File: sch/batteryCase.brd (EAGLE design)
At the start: 68.2 x 27.9 mm, 7 parts, among them X1 C-GRID-04-70553

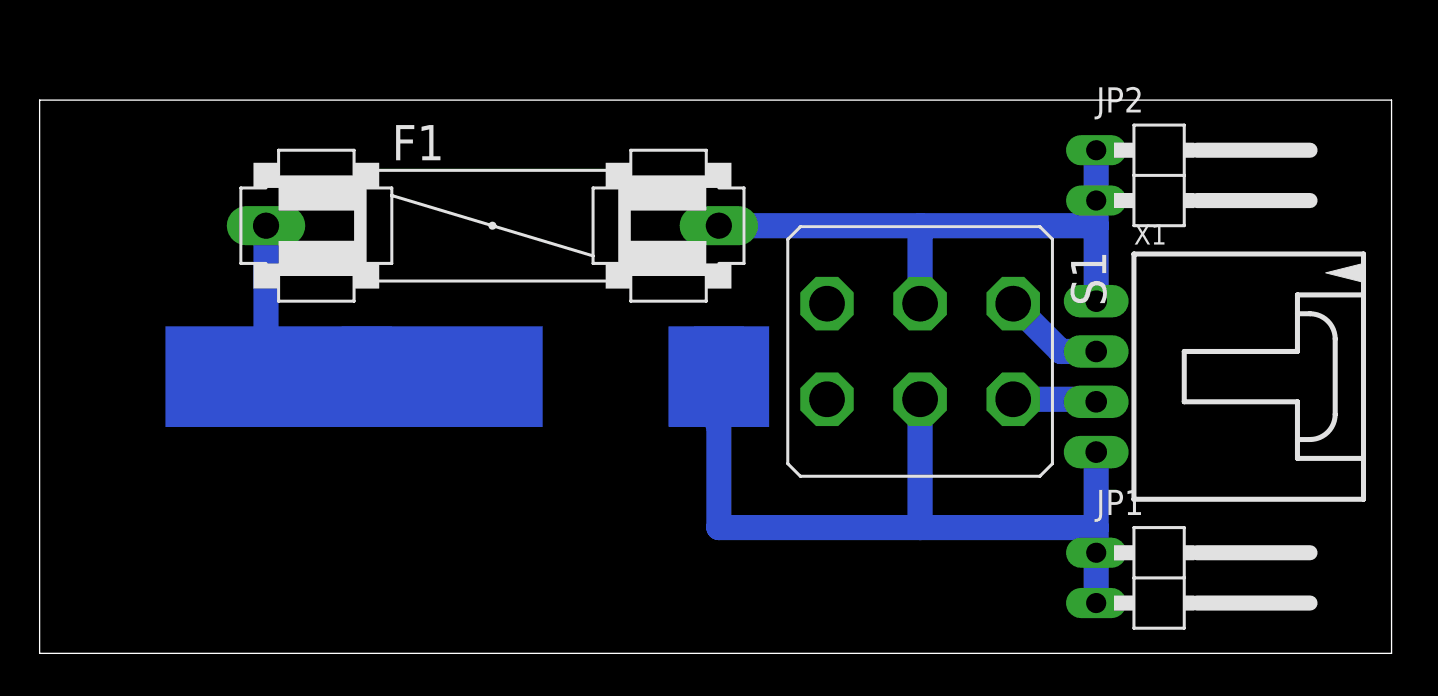
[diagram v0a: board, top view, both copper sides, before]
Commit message: Fine tuning the 3LR12 board layout
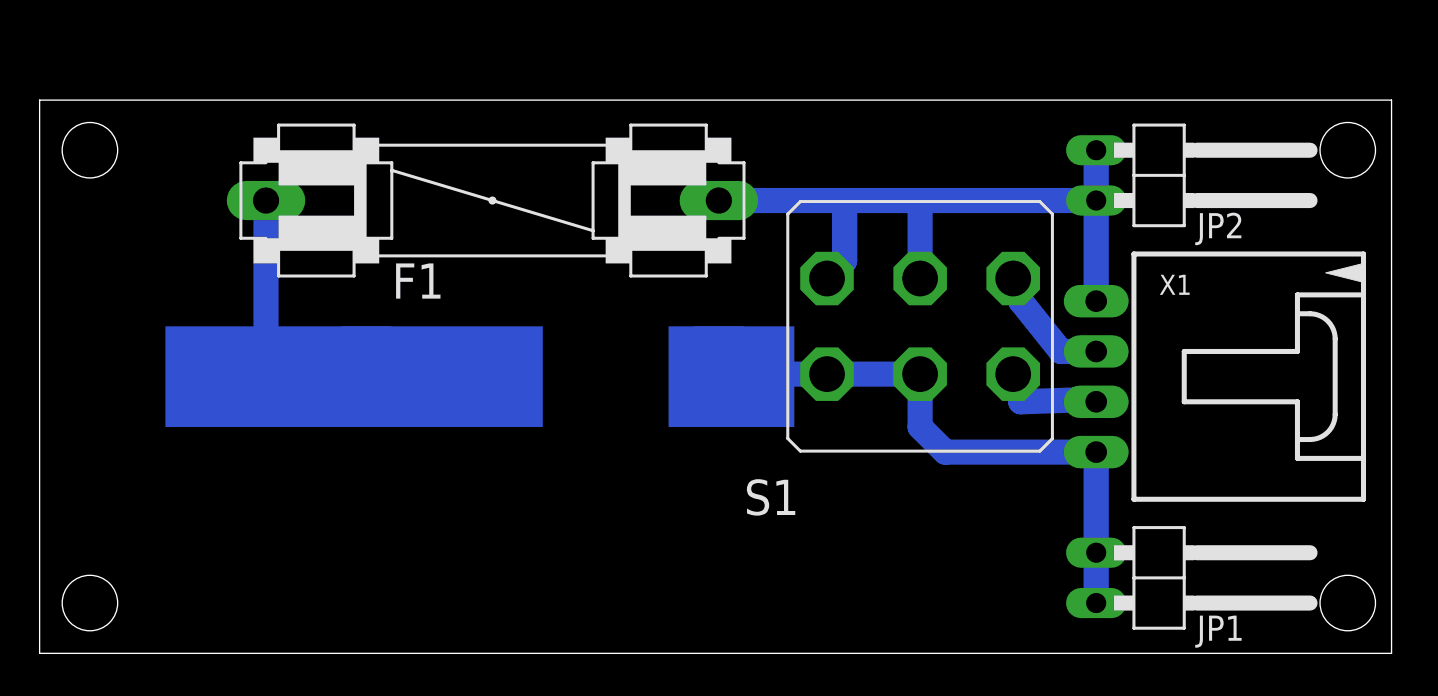
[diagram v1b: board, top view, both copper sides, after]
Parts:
- JP1: value FIXED GND -> LED!
- JP2: value FIXED PWR -> RUN!
- S1: value RUN -> RUN/LED
- moved S1 1.27 mm to (44.5, 16.5)
- moved F1 1.27 mm to (22.9, 22.9)
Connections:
- net N$2: now also S1.6
- net N$3: now also S1.3
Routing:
- net N$2: track 40.8 -> 29.9 mm
- net N$3: track 30.6 -> 34.9 mm
- net N$5: track 4.32 -> 5.72 mm
- net N$4: track 5.19 -> 6.55 mm
- net N$1: track 12.7 -> 14.0 mm
- removed copper zone on layer 16, net N$6
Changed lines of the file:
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@@
 <layer number="43" name="vRestrict" color="2" fill="10" visible="yes" active="yes"/>
 <layer number="44" name="Drills" color="7" fill="1" visible="no" active="yes"/>
-<layer number="45" name="Holes" color="7" fill="1" visible="no" active="yes"/>
+<layer number="45" name="Holes" color="7" fill="1" visible="yes" active="yes"/>
 <layer number="46" name="Milling" color="3" fill="1" visible="no" active="yes"/>
 <layer number="47" name="Measures" color="7" fill="1" visible="no" active="yes"/>
@@
 <wire x1="0" y1="27.93" x2="0" y2="0" width="0" layer="20"/>
 <rectangle x1="6.35" y1="11.43" x2="25.4" y2="16.51" layer="16"/>
-<rectangle x1="31.75" y1="11.43" x2="36.83" y2="16.51" layer="16"/>
+<rectangle x1="31.75" y1="11.43" x2="38.1" y2="16.51" layer="16"/>
+<hole x="2.54" y="2.54" drill="2.8"/>
+<hole x="2.54" y="25.4" drill="2.8"/>
+<hole x="66.04" y="2.54" drill="2.8"/>
+<hole x="66.04" y="25.4" drill="2.8"/>
 </plain>
 <attributes>
@@
 </autorouter>
 <elements>
-<element name="F1" library="special" package="FUSE" value="1A" x="22.86" y="21.59"/>
-<element name="JP1" library="pinhead" package="1X02/90" value="FIXED GND" x="57.15" y="3.81" rot="R270"/>
-<element name="JP2" library="pinhead" package="1X02/90" value="FIXED PWR" x="57.15" y="24.13" rot="R270"/>
+<element name="F1" library="special" package="FUSE" value="1A" x="22.86" y="22.86" smashed="yes">
+<attribute name="NAME" x="17.78" y="17.907" size="1.778" layer="25" ratio="10"/>
+<attribute name="VALUE" x="25.4" y="17.78" size="1.778" layer="27" ratio="10"/>
+</element>
+<element name="JP1" library="pinhead" package="1X02/90" value="LED!" x="57.15" y="3.81" smashed="yes" rot="R270">
+<attribute name="NAME" x="58.42" y="0.635" size="1.27" layer="25" ratio="10"/>
+<attribute name="VALUE" x="58.42" y="5.715" size="1.27" layer="27"/>
+</element>
+<element name="JP2" library="pinhead" package="1X02/90" value="RUN!" x="57.15" y="24.13" smashed="yes" rot="R270">
+<attribute name="NAME" x="58.42" y="20.955" size="1.27" layer="25" ratio="10"/>
+<attribute name="VALUE" x="58.42" y="26.035" size="1.27" layer="27"/>
+</element>
 <element name="PAD1" library="wirepad" package="SMD2,54-5,08" value="+4V5" x="16.51" y="13.97" rot="MR180"/>
 <element name="PAD2" library="wirepad" package="SMD2,54-5,08" value="0V" x="34.29" y="13.97" rot="MR0"/>
-<element name="S1" library="switch" package="M9040P2" value="RUN" x="44.45" y="15.24" rot="R270"/>
-<element name="X1" library="con-molex" package="70553-04" value="C-GRID-04-70553" x="60.96" y="13.97" rot="R270">
+<element name="S1" library="switch" package="M9040P2" value="RUN/LED" x="44.45" y="16.51" smashed="yes" rot="R270">
+<attribute name="NAME" x="35.56" y="6.985" size="1.778" layer="25" ratio="10"/>
+<attribute name="VALUE" x="40.005" y="6.985" size="1.778" layer="27" ratio="10"/>
+</element>
+<element name="X1" library="con-molex" package="70553-04" value="C-GRID-04-70553" x="60.96" y="13.97" smashed="yes" rot="R270">
 <attribute name="OC_NEWARK" value="unknown" x="60.96" y="13.97" size="1.778" layer="27" rot="R270" display="off"/>
 <attribute name="MF" value="" x="60.96" y="13.97" size="1.778" layer="27" rot="R270" display="off"/>
 <attribute name="MPN" value="" x="60.96" y="13.97" size="1.778" layer="27" rot="R270" display="off"/>
 <attribute name="OC_FARNELL" value="unknown" x="60.96" y="13.97" size="1.778" layer="27" rot="R270" display="off"/>
+<attribute name="NAME" x="56.515" y="18.0975" size="1.016" layer="25" ratio="10"/>
+<attribute name="VALUE" x="56.515" y="8.5725" size="0.8128" layer="27" ratio="10"/>
 </element>
 </elements>
@@
 <contactref element="F1" pad="1"/>
 <wire x1="16.51" y1="13.97" x2="11.43" y2="13.97" width="1.27" layer="16"/>
-<wire x1="11.43" y1="13.97" x2="11.43" y2="21.59" width="1.27" layer="16"/>
+<wire x1="11.43" y1="13.97" x2="11.43" y2="22.86" width="1.27" layer="16"/>
 </signal>
 <signal name="N$2">
@@
 <contactref element="JP1" pad="1"/>
 <wire x1="53.34" y1="2.54" x2="53.34" y2="5.08" width="1.27" layer="16"/>
-<wire x1="53.34" y1="5.08" x2="53.34" y2="6.35" width="1.27" layer="16"/>
-<wire x1="53.34" y1="6.35" x2="53.34" y2="10.16" width="1.27" layer="16"/>
+<wire x1="53.34" y1="5.08" x2="53.34" y2="10.16" width="1.27" layer="16"/>
 <contactref element="S1" pad="5"/>
-<wire x1="34.29" y1="6.35" x2="44.45" y2="6.35" width="1.27" layer="16"/>
-<wire x1="44.45" y1="6.35" x2="53.34" y2="6.35" width="1.27" layer="16"/>
-<wire x1="34.29" y1="13.97" x2="34.29" y2="6.35" width="1.27" layer="16"/>
-<wire x1="44.45" y1="12.827" x2="44.45" y2="6.35" width="1.27" layer="16"/>
+<contactref element="S1" pad="6"/>
+<wire x1="39.751" y1="14.097" x2="34.417" y2="14.097" width="1.27" layer="16"/>
+<wire x1="34.417" y1="14.097" x2="34.29" y2="13.97" width="1.27" layer="16"/>
+<wire x1="39.751" y1="14.097" x2="44.45" y2="14.097" width="1.27" layer="16"/>
+<wire x1="44.45" y1="14.097" x2="44.45" y2="11.43" width="1.27" layer="16"/>
+<wire x1="44.45" y1="11.43" x2="45.72" y2="10.16" width="1.27" layer="16"/>
+<wire x1="45.72" y1="10.16" x2="53.34" y2="10.16" width="1.27" layer="16"/>
 </signal>
 <signal name="N$3">
@@
 <contactref element="JP2" pad="2"/>
 <wire x1="53.34" y1="25.4" x2="53.34" y2="22.86" width="1.27" layer="16"/>
-<wire x1="53.34" y1="22.86" x2="53.34" y2="21.59" width="1.27" layer="16"/>
-<wire x1="53.34" y1="21.59" x2="53.34" y2="17.78" width="1.27" layer="16"/>
+<wire x1="53.34" y1="22.86" x2="53.34" y2="17.78" width="1.27" layer="16"/>
 <contactref element="S1" pad="2"/>
-<wire x1="34.29" y1="21.59" x2="44.45" y2="21.59" width="1.27" layer="16"/>
-<wire x1="44.45" y1="21.59" x2="53.34" y2="21.59" width="1.27" layer="16"/>
-<wire x1="44.45" y1="21.59" x2="44.45" y2="17.653" width="1.27" layer="16"/>
+<wire x1="34.29" y1="22.86" x2="40.64" y2="22.86" width="1.27" layer="16"/>
+<wire x1="40.64" y1="22.86" x2="44.45" y2="22.86" width="1.27" layer="16"/>
+<wire x1="44.45" y1="22.86" x2="53.34" y2="22.86" width="1.27" layer="16"/>
+<wire x1="44.45" y1="22.86" x2="44.45" y2="18.923" width="1.27" layer="16"/>
+<contactref element="S1" pad="3"/>
+<wire x1="39.751" y1="18.923" x2="40.64" y2="19.812" width="1.27" layer="16"/>
+<wire x1="40.64" y1="19.812" x2="40.64" y2="22.86" width="1.27" layer="16"/>
 </signal>
 <signal name="N$4">
 <contactref element="X1" pad="2"/>
 <contactref element="S1" pad="1"/>
-<wire x1="49.149" y1="17.653" x2="51.562" y2="15.24" width="1.27" layer="16"/>
+<wire x1="49.149" y1="18.923" x2="49.53" y2="18.923" width="1.27" layer="16"/>
+<wire x1="49.53" y1="18.923" x2="49.53" y2="17.78" width="1.27" layer="16"/>
+<wire x1="49.53" y1="17.78" x2="51.562" y2="15.24" width="1.27" layer="16"/>
 <wire x1="51.562" y1="15.24" x2="53.34" y2="15.24" width="1.27" layer="16"/>
 </signal>
@@
 <contactref element="S1" pad="4"/>
 <wire x1="53.34" y1="12.7" x2="53.34" y2="12.827" width="1.27" layer="16"/>
-<wire x1="53.34" y1="12.827" x2="49.149" y2="12.827" width="1.27" layer="16"/>
-</signal>
-<signal name="N$6">
-<polygon width="0" layer="16" isolate="0.4064">
-<vertex x="34.29" y="13.97"/>
-<vertex x="34.29" y="8.89"/>
-<vertex x="33.02" y="13.97"/>
-</polygon>
+<wire x1="53.34" y1="12.827" x2="49.53" y2="12.7" width="1.27" layer="16"/>
+<wire x1="49.53" y1="12.7" x2="49.53" y2="14.097" width="1.27" layer="16"/>
+<wire x1="49.53" y1="14.097" x2="49.149" y2="14.097" width="1.27" layer="16"/>
 </signal>
 </signals>

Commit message: Better fuse holder and clearances
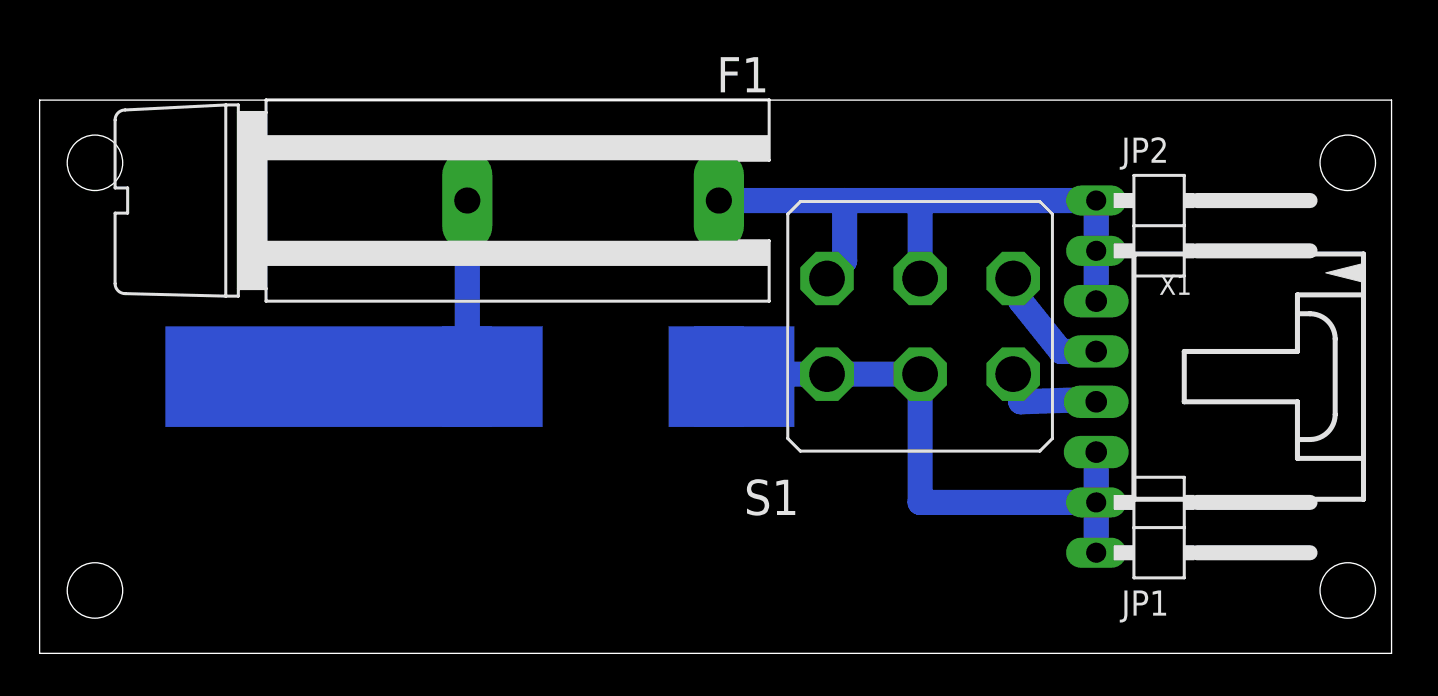
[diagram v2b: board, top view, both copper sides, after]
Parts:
- F1: value 1A -> FUSEKS10H; device special:FUSE -> fuse:KS10H
- moved F1 6.35 mm to (29.2, 22.9), turned to 90 degrees
- moved PAD1 5.08 mm to (21.6, 14.0)
- moved JP1 2.54 mm to (57.1, 6.35)
- moved JP2 2.54 mm to (57.1, 21.6)
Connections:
- net N$1: now also F1.2; no longer F1.1
- net N$3: now also F1.1; no longer F1.2
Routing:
- net N$1: track 14.0 -> 8.89 mm
- net N$3: track 34.9 -> 32.4 mm
- net N$2: track 29.9 -> 30.7 mm
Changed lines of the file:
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@@
 <rectangle x1="6.35" y1="11.43" x2="25.4" y2="16.51" layer="16"/>
 <rectangle x1="31.75" y1="11.43" x2="38.1" y2="16.51" layer="16"/>
-<hole x="2.54" y="2.54" drill="2.8"/>
-<hole x="2.54" y="25.4" drill="2.8"/>
-<hole x="66.04" y="2.54" drill="2.8"/>
-<hole x="66.04" y="25.4" drill="2.8"/>
+<hole x="2.794" y="3.175" drill="2.8"/>
+<hole x="2.794" y="24.765" drill="2.8"/>
+<hole x="66.04" y="3.175" drill="2.8"/>
+<hole x="66.04" y="24.765" drill="2.8"/>
 </plain>
 <attributes>
@@
 </autorouter>
 <elements>
-<element name="F1" library="special" package="FUSE" value="1A" x="22.86" y="22.86" smashed="yes">
-<attribute name="NAME" x="17.78" y="17.907" size="1.778" layer="25" ratio="10"/>
-<attribute name="VALUE" x="25.4" y="17.78" size="1.778" layer="27" ratio="10"/>
-</element>
-<element name="JP1" library="pinhead" package="1X02/90" value="LED!" x="57.15" y="3.81" smashed="yes" rot="R270">
-<attribute name="NAME" x="58.42" y="0.635" size="1.27" layer="25" ratio="10"/>
-<attribute name="VALUE" x="58.42" y="5.715" size="1.27" layer="27"/>
-</element>
-<element name="JP2" library="pinhead" package="1X02/90" value="RUN!" x="57.15" y="24.13" smashed="yes" rot="R270">
-<attribute name="NAME" x="58.42" y="20.955" size="1.27" layer="25" ratio="10"/>
-<attribute name="VALUE" x="58.42" y="26.035" size="1.27" layer="27"/>
-</element>
-<element name="PAD1" library="wirepad" package="SMD2,54-5,08" value="+4V5" x="16.51" y="13.97" rot="MR180"/>
+<element name="JP1" library="pinhead" package="1X02/90" value="LED!" x="57.15" y="6.35" smashed="yes" rot="R270">
+<attribute name="NAME" x="54.61" y="1.905" size="1.27" layer="25" ratio="10"/>
+<attribute name="VALUE" x="58.42" y="3.175" size="1.27" layer="27"/>
+</element>
+<element name="JP2" library="pinhead" package="1X02/90" value="RUN!" x="57.15" y="21.59" smashed="yes" rot="R270">
+<attribute name="NAME" x="54.61" y="24.765" size="1.27" layer="25" ratio="10"/>
+<attribute name="VALUE" x="58.42" y="23.495" size="1.27" layer="27"/>
+</element>
+<element name="PAD1" library="wirepad" package="SMD2,54-5,08" value="+4V5" x="21.59" y="13.97" rot="MR180"/>
 <element name="PAD2" library="wirepad" package="SMD2,54-5,08" value="0V" x="34.29" y="13.97" rot="MR0"/>
 <element name="S1" library="switch" package="M9040P2" value="RUN/LED" x="44.45" y="16.51" smashed="yes" rot="R270">
@@
 <attribute name="VALUE" x="56.515" y="8.5725" size="0.8128" layer="27" ratio="10"/>
 </element>
+<element name="F1" library="fuse" package="KS10H" value="FUSEKS10H" x="29.21" y="22.86" rot="R90">
+<attribute name="OC_NEWARK" value="unknown" x="29.21" y="22.86" size="1.778" layer="27" rot="R90" display="off"/>
+<attribute name="MF" value="" x="29.21" y="22.86" size="1.778" layer="27" rot="R90" display="off"/>
+<attribute name="MPN" value="" x="29.21" y="22.86" size="1.778" layer="27" rot="R90" display="off"/>
+<attribute name="OC_FARNELL" value="unknown" x="29.21" y="22.86" size="1.778" layer="27" rot="R90" display="off"/>
+</element>
 </elements>
 <signals>
-<signal name="N$1">
-<contactref element="PAD1" pad="1"/>
-<contactref element="F1" pad="1"/>
-<wire x1="16.51" y1="13.97" x2="11.43" y2="13.97" width="1.27" layer="16"/>
-<wire x1="11.43" y1="13.97" x2="11.43" y2="22.86" width="1.27" layer="16"/>
-</signal>
 <signal name="N$2">
 <contactref element="PAD2" pad="1"/>
@@
 <contactref element="X1" pad="4"/>
 <contactref element="JP1" pad="1"/>
-<wire x1="53.34" y1="2.54" x2="53.34" y2="5.08" width="1.27" layer="16"/>
-<wire x1="53.34" y1="5.08" x2="53.34" y2="10.16" width="1.27" layer="16"/>
+<wire x1="53.34" y1="5.08" x2="53.34" y2="7.62" width="1.27" layer="16"/>
 <contactref element="S1" pad="5"/>
 <contactref element="S1" pad="6"/>
@@
 <wire x1="34.417" y1="14.097" x2="34.29" y2="13.97" width="1.27" layer="16"/>
 <wire x1="39.751" y1="14.097" x2="44.45" y2="14.097" width="1.27" layer="16"/>
-<wire x1="44.45" y1="14.097" x2="44.45" y2="11.43" width="1.27" layer="16"/>
-<wire x1="44.45" y1="11.43" x2="45.72" y2="10.16" width="1.27" layer="16"/>
-<wire x1="45.72" y1="10.16" x2="53.34" y2="10.16" width="1.27" layer="16"/>
+<wire x1="44.45" y1="14.097" x2="44.45" y2="7.62" width="1.27" layer="16"/>
+<wire x1="44.45" y1="7.62" x2="53.34" y2="7.62" width="1.27" layer="16"/>
+<wire x1="53.34" y1="7.62" x2="53.34" y2="10.16" width="1.27" layer="16"/>
 </signal>
 <signal name="N$3">
-<contactref element="F1" pad="2"/>
 <contactref element="JP2" pad="1"/>
 <contactref element="X1" pad="1"/>
 <contactref element="JP2" pad="2"/>
-<wire x1="53.34" y1="25.4" x2="53.34" y2="22.86" width="1.27" layer="16"/>
-<wire x1="53.34" y1="22.86" x2="53.34" y2="17.78" width="1.27" layer="16"/>
+<wire x1="53.34" y1="20.32" x2="53.34" y2="17.78" width="1.27" layer="16"/>
 <contactref element="S1" pad="2"/>
-<wire x1="34.29" y1="22.86" x2="40.64" y2="22.86" width="1.27" layer="16"/>
 <wire x1="40.64" y1="22.86" x2="44.45" y2="22.86" width="1.27" layer="16"/>
 <wire x1="44.45" y1="22.86" x2="53.34" y2="22.86" width="1.27" layer="16"/>
+<wire x1="53.34" y1="22.86" x2="53.34" y2="20.32" width="1.27" layer="16"/>
 <wire x1="44.45" y1="22.86" x2="44.45" y2="18.923" width="1.27" layer="16"/>
 <contactref element="S1" pad="3"/>
 <wire x1="39.751" y1="18.923" x2="40.64" y2="19.812" width="1.27" layer="16"/>
 <wire x1="40.64" y1="19.812" x2="40.64" y2="22.86" width="1.27" layer="16"/>
+<contactref element="F1" pad="1"/>
+<wire x1="34.29" y1="22.86" x2="40.64" y2="22.86" width="1.27" layer="16"/>
 </signal>
 <signal name="N$4">
@@
 <wire x1="49.53" y1="14.097" x2="49.149" y2="14.097" width="1.27" layer="16"/>
 </signal>
+<signal name="N$1">
+<contactref element="PAD1" pad="1"/>
+<contactref element="F1" pad="2"/>
+<wire x1="21.59" y1="22.86" x2="21.59" y2="13.97" width="1.27" layer="16"/>
+</signal>
 </signals>
